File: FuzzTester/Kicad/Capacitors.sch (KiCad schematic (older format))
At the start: 10 parts, among them U4 CD4051B

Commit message: PCB fixes
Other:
- moved on the sheet: C12, C13, C14, C15, C16, C17, C18, C19

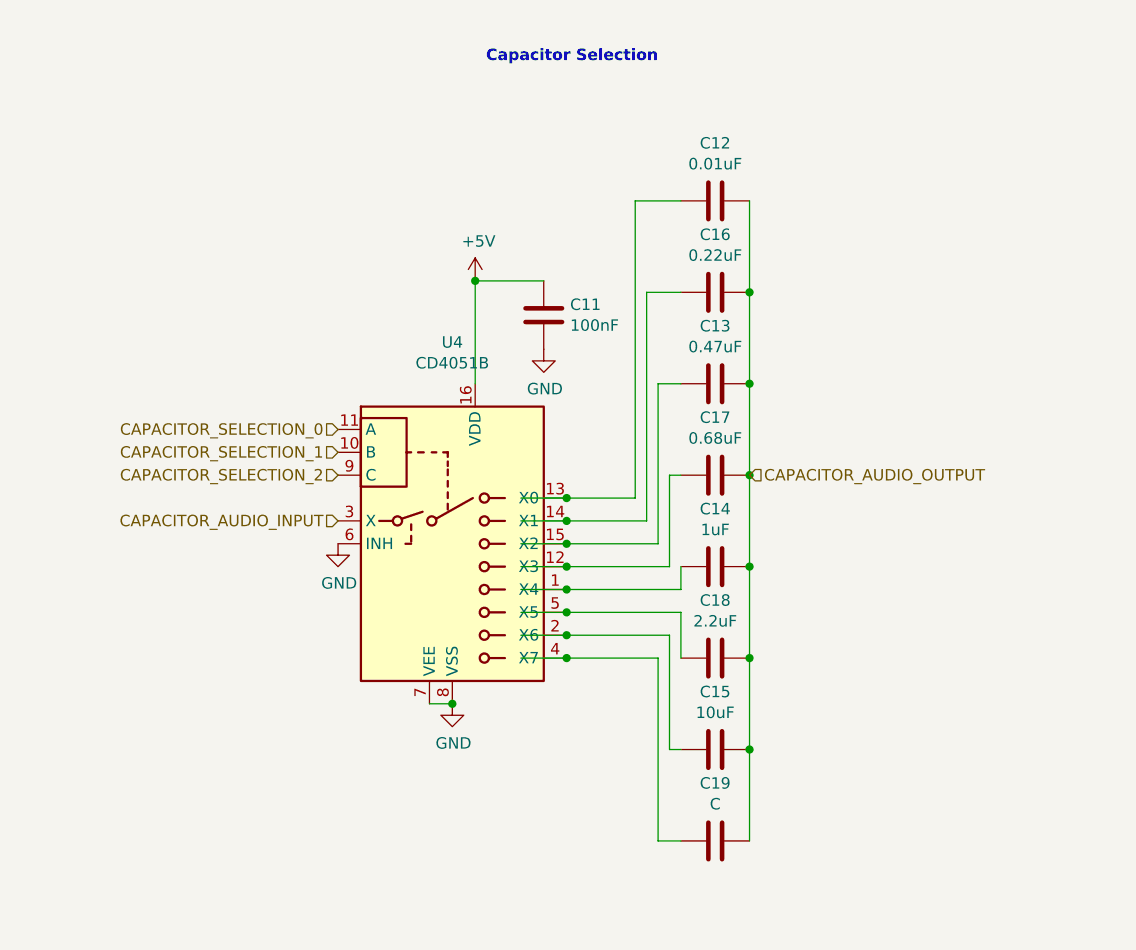
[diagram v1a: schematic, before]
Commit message: Changed power supply
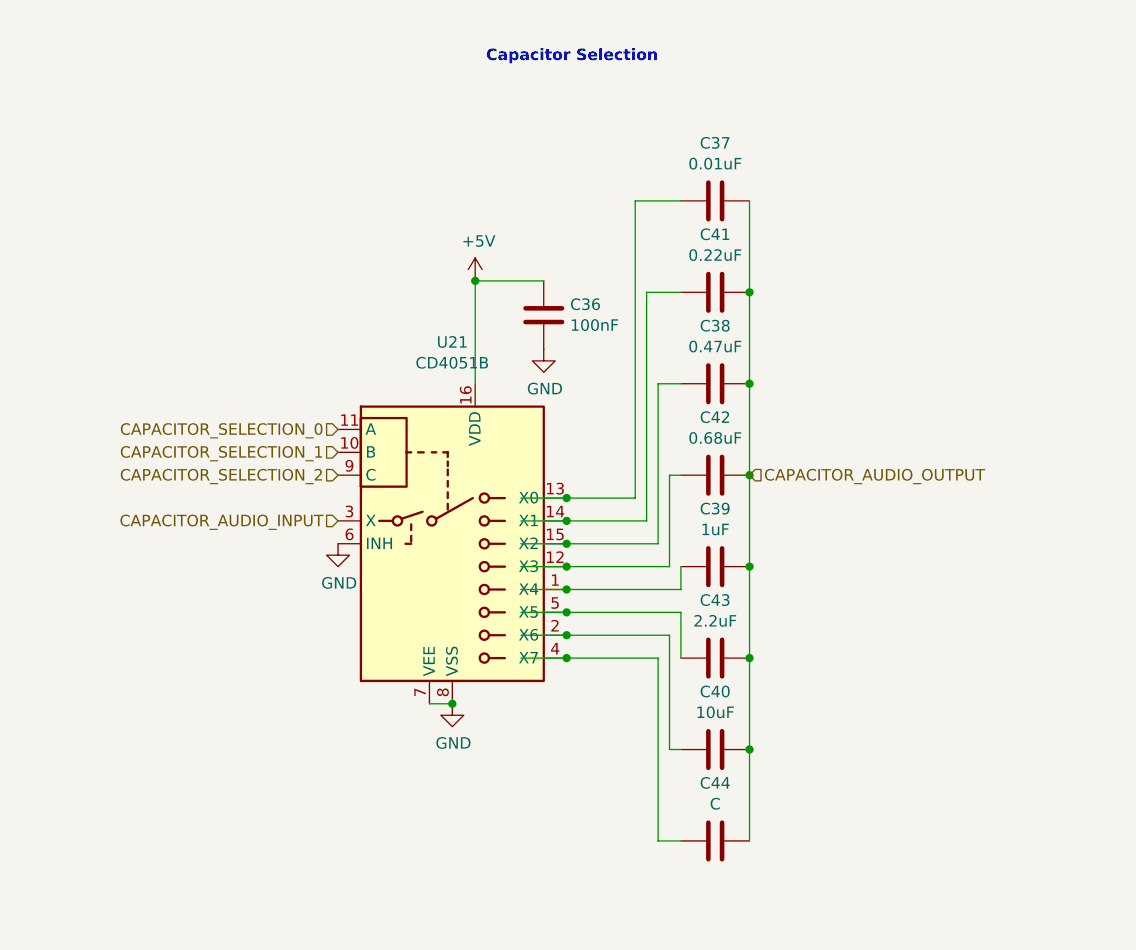
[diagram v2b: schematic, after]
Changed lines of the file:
@@
 $Descr A4 11693 8268
 encoding utf-8
-Sheet 5 10
+Sheet 8 10
 Title "Guitar Pedal Effect Fuzz Digitally Controlled"
 Date ""
@@
 AR Path="/5E983DF3/5E9AD56C" Ref="U4"  Part="1"
 AR Path="/5F9F739D/5E9AD56C" Ref="U21"  Part="1"
-F 0 "U4" H 4350 4631 50  0000 C CNN
+F 0 "U21" H 4350 4631 50  0000 C CNN
 F 1 "CD4051B" H 4350 4540 50  0000 C CNN
 F 2 "Package_SO:SOIC-16_3.9x9.9mm_P1.27mm" H 4500 3000 50  0001 L CNN
@@
 AR Path="/5E983DF3/5E9AD572" Ref="C17"  Part="1"
 AR Path="/5F9F739D/5E9AD572" Ref="C42"  Part="1"
-F 0 "C17" V 5248 3450 50  0000 C CNN
+F 0 "C42" V 5248 3450 50  0000 C CNN
 F 1 "0.68uF" V 5339 3450 50  0000 C CNN
 F 2 "Capacitor_SMD:C_0805_2012Metric_Pad1.15x1.40mm_HandSolder" H 5538 3300 50  0001 C CNN
@@
 AR Path="/5E983DF3/5E9AD584" Ref="C16"  Part="1"
 AR Path="/5F9F739D/5E9AD584" Ref="C41"  Part="1"
-F 0 "C16" V 5248 2650 50  0000 C CNN
+F 0 "C41" V 5248 2650 50  0000 C CNN
 F 1 "0.22uF" V 5339 2650 50  0000 C CNN
 F 2 "Capacitor_SMD:C_0805_2012Metric_Pad1.15x1.40mm_HandSolder" H 5538 2500 50  0001 C CNN
@@
 AR Path="/5E983DF3/5E9AD58A" Ref="C14"  Part="1"
 AR Path="/5F9F739D/5E9AD58A" Ref="C39"  Part="1"
-F 0 "C14" V 5248 3850 50  0000 C CNN
+F 0 "C39" V 5248 3850 50  0000 C CNN
 F 1 "1uF" V 5339 3850 50  0000 C CNN
 F 2 "Capacitor_SMD:C_0805_2012Metric_Pad1.15x1.40mm_HandSolder" H 5538 3700 50  0001 C CNN
@@
 AR Path="/5E983DF3/5E9AD596" Ref="C13"  Part="1"
 AR Path="/5F9F739D/5E9AD596" Ref="C38"  Part="1"
-F 0 "C13" V 5248 3050 50  0000 C CNN
+F 0 "C38" V 5248 3050 50  0000 C CNN
 F 1 "0.47uF" V 5339 3050 50  0000 C CNN
 F 2 "Capacitor_SMD:C_0805_2012Metric_Pad1.15x1.40mm_HandSolder" H 5538 2900 50  0001 C CNN
@@
 AR Path="/5E983DF3/5E9AD59F" Ref="C11"  Part="1"
 AR Path="/5F9F739D/5E9AD59F" Ref="C36"  Part="1"
-F 0 "C11" H 4865 2796 50  0000 L CNN
+F 0 "C36" H 4865 2796 50  0000 L CNN
 F 1 "100nF" H 4865 2705 50  0000 L CNN
 F 2 "Capacitor_SMD:C_0805_2012Metric_Pad1.15x1.40mm_HandSolder" H 4788 2600 50  0001 C CNN
@@
 AR Path="/5E983DF3/5E9AD5A6" Ref="#PWR030"  Part="1"
 AR Path="/5F9F739D/5E9AD5A6" Ref="#PWR0100"  Part="1"
-F 0 "#PWR030" H 4450 2450 50  0001 C CNN
+F 0 "#PWR0100" H 4450 2450 50  0001 C CNN
 F 1 "+5V" H 4465 2773 50  0000 C CNN
 F 2 "" H 4450 2600 50  0001 C CNN
@@
 AR Path="/5E983DF3/5E9AD5AC" Ref="#PWR031"  Part="1"
 AR Path="/5F9F739D/5E9AD5AC" Ref="#PWR0101"  Part="1"
-F 0 "#PWR031" H 4750 2650 50  0001 C CNN
+F 0 "#PWR0101" H 4750 2650 50  0001 C CNN
 F 1 "GND" H 4755 2727 50  0000 C CNN
 F 2 "" H 4750 2900 50  0001 C CNN
@@
 AR Path="/5E983DF3/5E9AD5B2" Ref="#PWR029"  Part="1"
 AR Path="/5F9F739D/5E9AD5B2" Ref="#PWR099"  Part="1"
-F 0 "#PWR029" H 4350 4200 50  0001 C CNN
+F 0 "#PWR099" H 4350 4200 50  0001 C CNN
 F 1 "GND" H 4355 4277 50  0000 C CNN
 F 2 "" H 4350 4450 50  0001 C CNN
@@
 AR Path="/5E983DF3/5E9AD5C3" Ref="#PWR028"  Part="1"
 AR Path="/5F9F739D/5E9AD5C3" Ref="#PWR098"  Part="1"
-F 0 "#PWR028" H 3850 3500 50  0001 C CNN
+F 0 "#PWR098" H 3850 3500 50  0001 C CNN
 F 1 "GND" H 3855 3577 50  0000 C CNN
 F 2 "" H 3850 3750 50  0001 C CNN
@@
 AR Path="/5E983DF3/5E9AD590" Ref="C12"  Part="1"
 AR Path="/5F9F739D/5E9AD590" Ref="C37"  Part="1"
-F 0 "C12" V 5248 2250 50  0000 C CNN
+F 0 "C37" V 5248 2250 50  0000 C CNN
 F 1 "0.01uF" V 5339 2250 50  0000 C CNN
 F 2 "Capacitor_SMD:C_0805_2012Metric_Pad1.15x1.40mm_HandSolder" H 5538 2100 50  0001 C CNN
@@
 AR Path="/5E983DF3/5E9AD57E" Ref="C15"  Part="1"
 AR Path="/5F9F739D/5E9AD57E" Ref="C40"  Part="1"
-F 0 "C15" V 5248 4650 50  0000 C CNN
+F 0 "C40" V 5248 4650 50  0000 C CNN
 F 1 "10uF" V 5339 4650 50  0000 C CNN
 F 2 "Capacitor_SMD:C_0805_2012Metric_Pad1.15x1.40mm_HandSolder" H 5538 4500 50  0001 C CNN
@@
 AR Path="/5E983DF3/5E9AD5F3" Ref="C19"  Part="1"
 AR Path="/5F9F739D/5E9AD5F3" Ref="C44"  Part="1"
-F 0 "C19" V 5248 5050 50  0000 C CNN
+F 0 "C44" V 5248 5050 50  0000 C CNN
 F 1 "C" V 5339 5050 50  0000 C CNN
 F 2 "Capacitor_SMD:C_0805_2012Metric_Pad1.15x1.40mm_HandSolder" H 5538 4900 50  0001 C CNN
@@
 AR Path="/5E983DF3/5E9AD578" Ref="C18"  Part="1"
 AR Path="/5F9F739D/5E9AD578" Ref="C43"  Part="1"
-F 0 "C18" V 5248 4250 50  0000 C CNN
+F 0 "C43" V 5248 4250 50  0000 C CNN
 F 1 "2.2uF" V 5339 4250 50  0000 C CNN
 F 2 "Capacitor_SMD:C_0805_2012Metric_Pad1.15x1.40mm_HandSolder" H 5538 4100 50  0001 C CNN

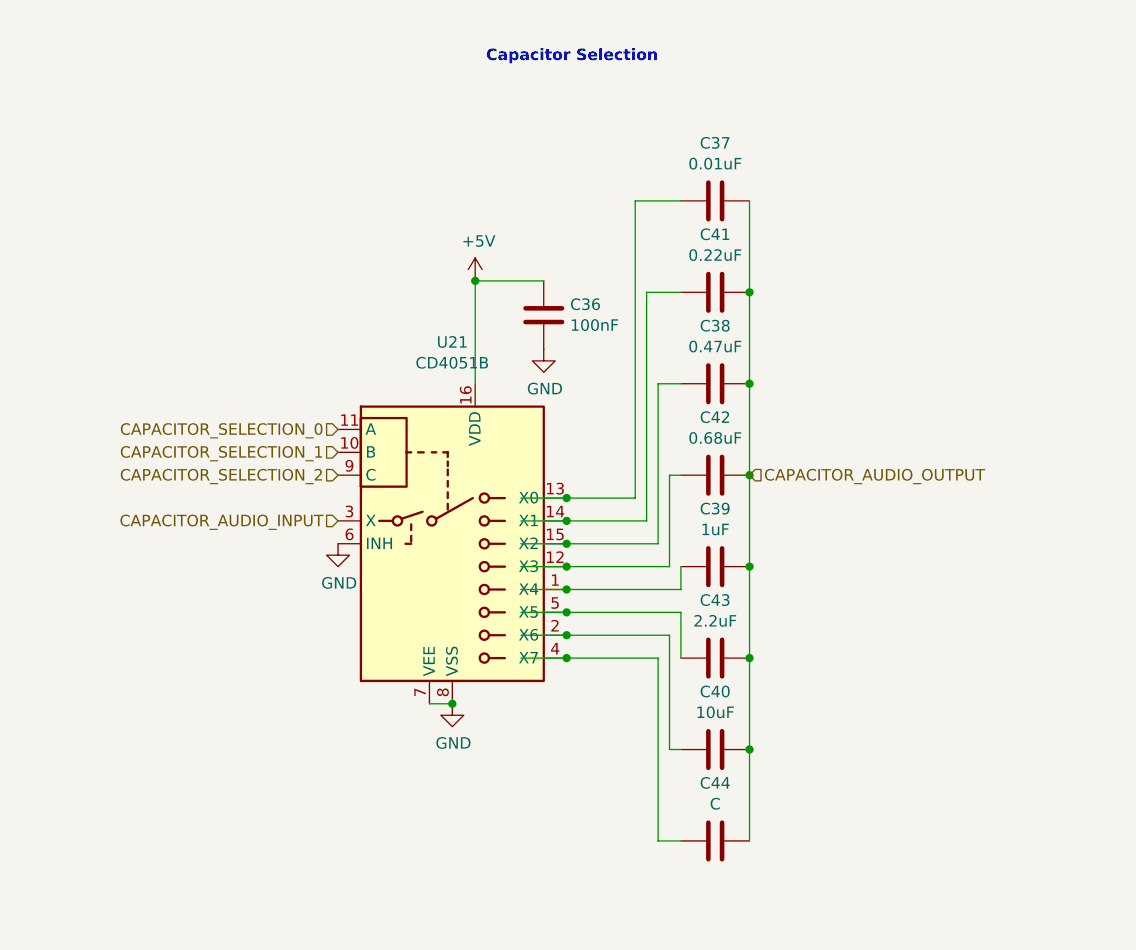
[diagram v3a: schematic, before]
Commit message: Power regulator -9V
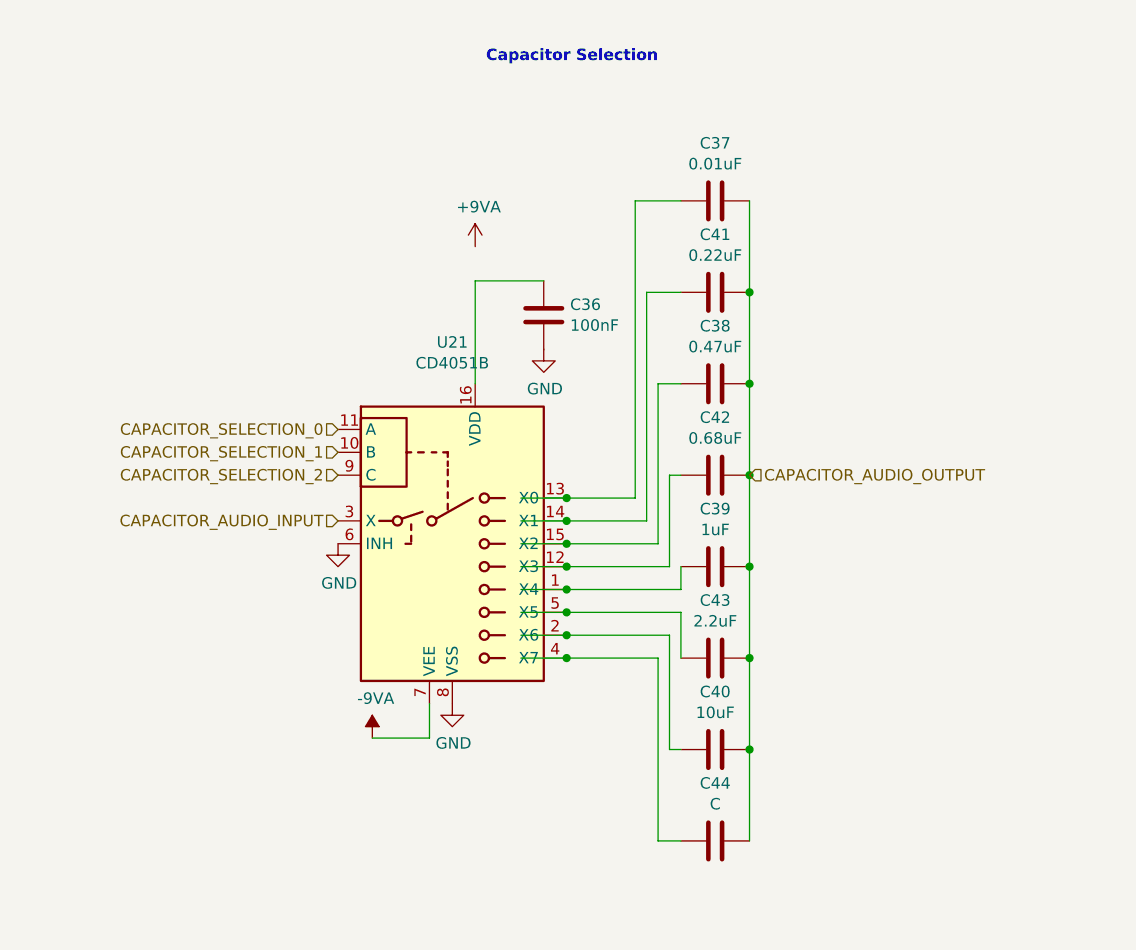
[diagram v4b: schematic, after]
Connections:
- net labels added: +9VA, -9VA
- net labels removed: +5V
- wire segments 40 -> 41
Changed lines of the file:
@@
 $Descr A4 11693 8268
 encoding utf-8
-Sheet 5 9
+Sheet 3 9
 Title "Guitar Pedal Effect Fuzz Digitally Controlled"
 Date "2020-04-07"
@@
 	1    0    0    -1
 $EndComp
-Connection ~ 4450 2600
-$Comp
-L power:+5V #PWR?
-U 1 1 5E9AD5A6
-P 4450 2600
-AR Path="/5E87C69B/5E9AD5A6" Ref="#PWR?"  Part="1"
-AR Path="/5E984186/5E9AD5A6" Ref="#PWR?"  Part="1"
-AR Path="/5E983DF3/5E9AD5A6" Ref="#PWR030"  Part="1"
-AR Path="/5F9F739D/5E9AD5A6" Ref="#PWR0100"  Part="1"
-F 0 "#PWR0100" H 4450 2450 50  0001 C CNN
-F 1 "+5V" H 4465 2773 50  0000 C CNN
-F 2 "" H 4450 2600 50  0001 C CNN
-F 3 "" H 4450 2600 50  0001 C CNN
-	1    4450 2600
-	1    0    0    -1
-$EndComp
 $Comp
 L power:GND #PWR?
@@
 	1    0    0    -1
 $EndComp
-Wire Wire Line
-	4250 4450 4350 4450
-Connection ~ 4350 4450
 $Comp
 L power:GND #PWR?
@@
 Wire Wire Line
 	4850 4250 5250 4250
+$Comp
+L power:-9VA #PWR0116
+U 1 1 5E9087E5
+P 4000 4600
+AR Path="/5E983DF3/5E9087E5" Ref="#PWR0116"  Part="1"
+AR Path="/5F9F739D/5E9087E5" Ref="#PWR0118"  Part="1"
+F 0 "#PWR0118" H 4000 4475 50  0001 C CNN
+F 1 "-9VA" H 4015 4773 50  0000 C CNN
+F 2 "" H 4000 4600 50  0001 C CNN
+F 3 "" H 4000 4600 50  0001 C CNN
+	1    4000 4600
+	1    0    0    -1
+$EndComp
+$Comp
+L power:+9VA #PWR0117
+U 1 1 5E916795
+P 4450 2450
+AR Path="/5E983DF3/5E916795" Ref="#PWR0117"  Part="1"
+AR Path="/5F9F739D/5E916795" Ref="#PWR0119"  Part="1"
+F 0 "#PWR0119" H 4450 2325 50  0001 C CNN
+F 1 "+9VA" H 4465 2623 50  0000 C CNN
+F 2 "" H 4450 2450 50  0001 C CNN
+F 3 "" H 4450 2450 50  0001 C CNN
+	1    4450 2450
+	1    0    0    -1
+$EndComp
+Wire Wire Line
+	4250 4450 4250 4600
+Wire Wire Line
+	4250 4600 4000 4600
 $EndSCHEMATC

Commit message: PCB Placement 100x82
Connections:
- net labels added: +9V
- net labels removed: +9VA, -9VA
- wire segments 41 -> 32
